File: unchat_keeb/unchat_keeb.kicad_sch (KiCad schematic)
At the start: 11 parts, among them U1 74HC365, U2 74HC365, U3 74HC365, U4 74HC365, U5 74HC365, U6 74HC365, U99 Raspberry_Pi_Pico

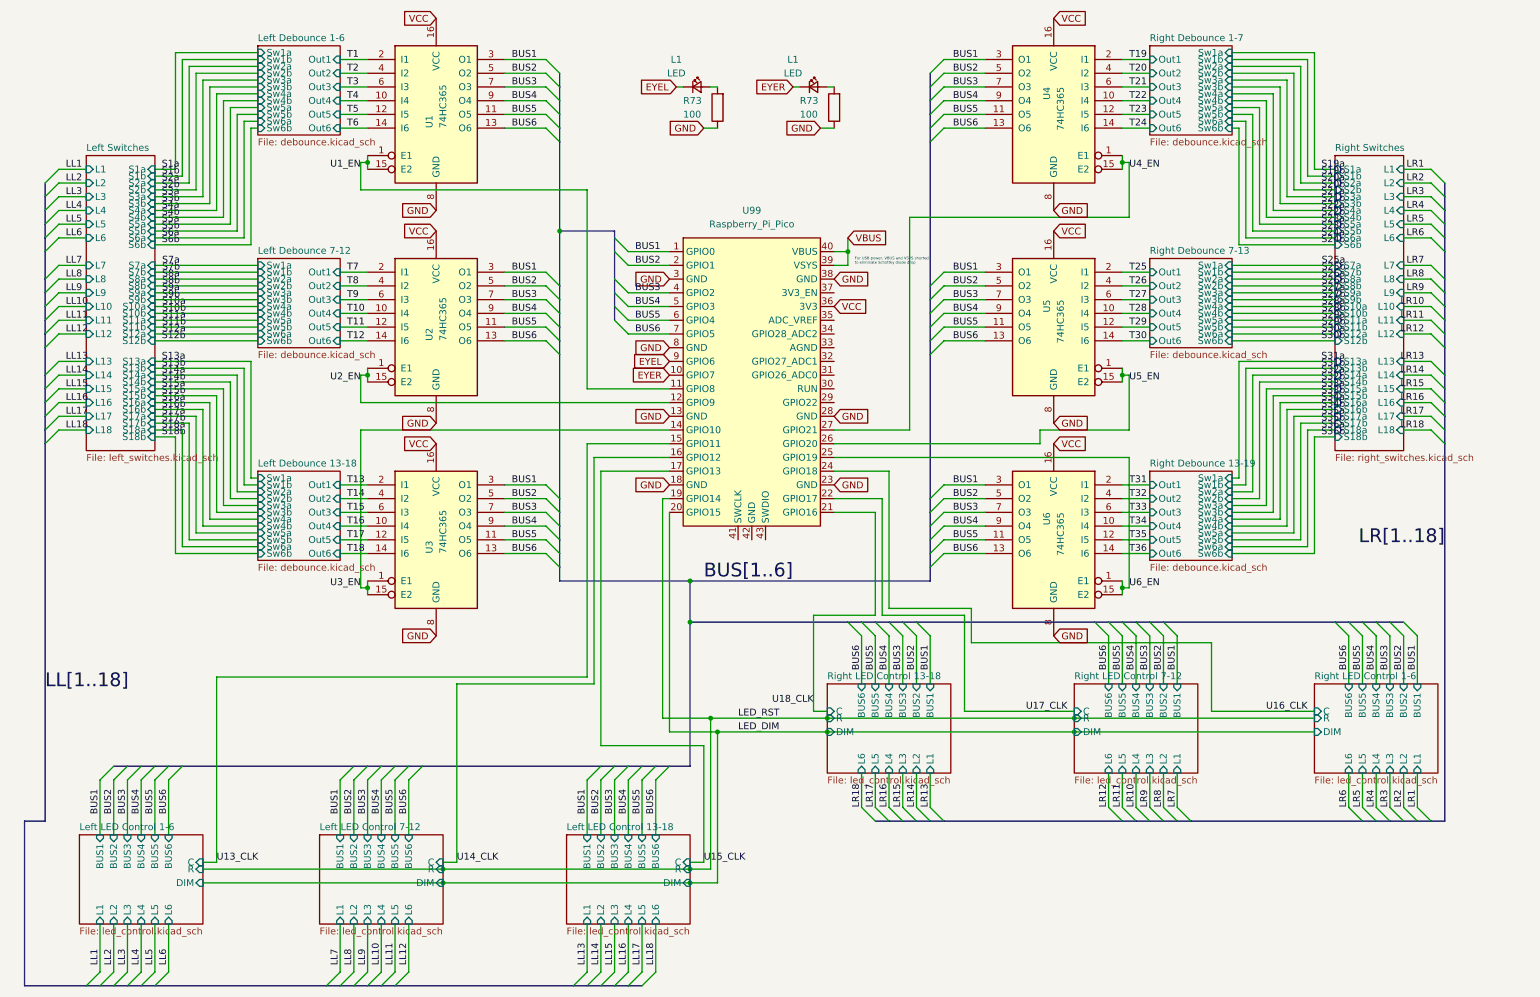
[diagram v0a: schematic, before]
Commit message: Add extra columns, updating to 42-key design
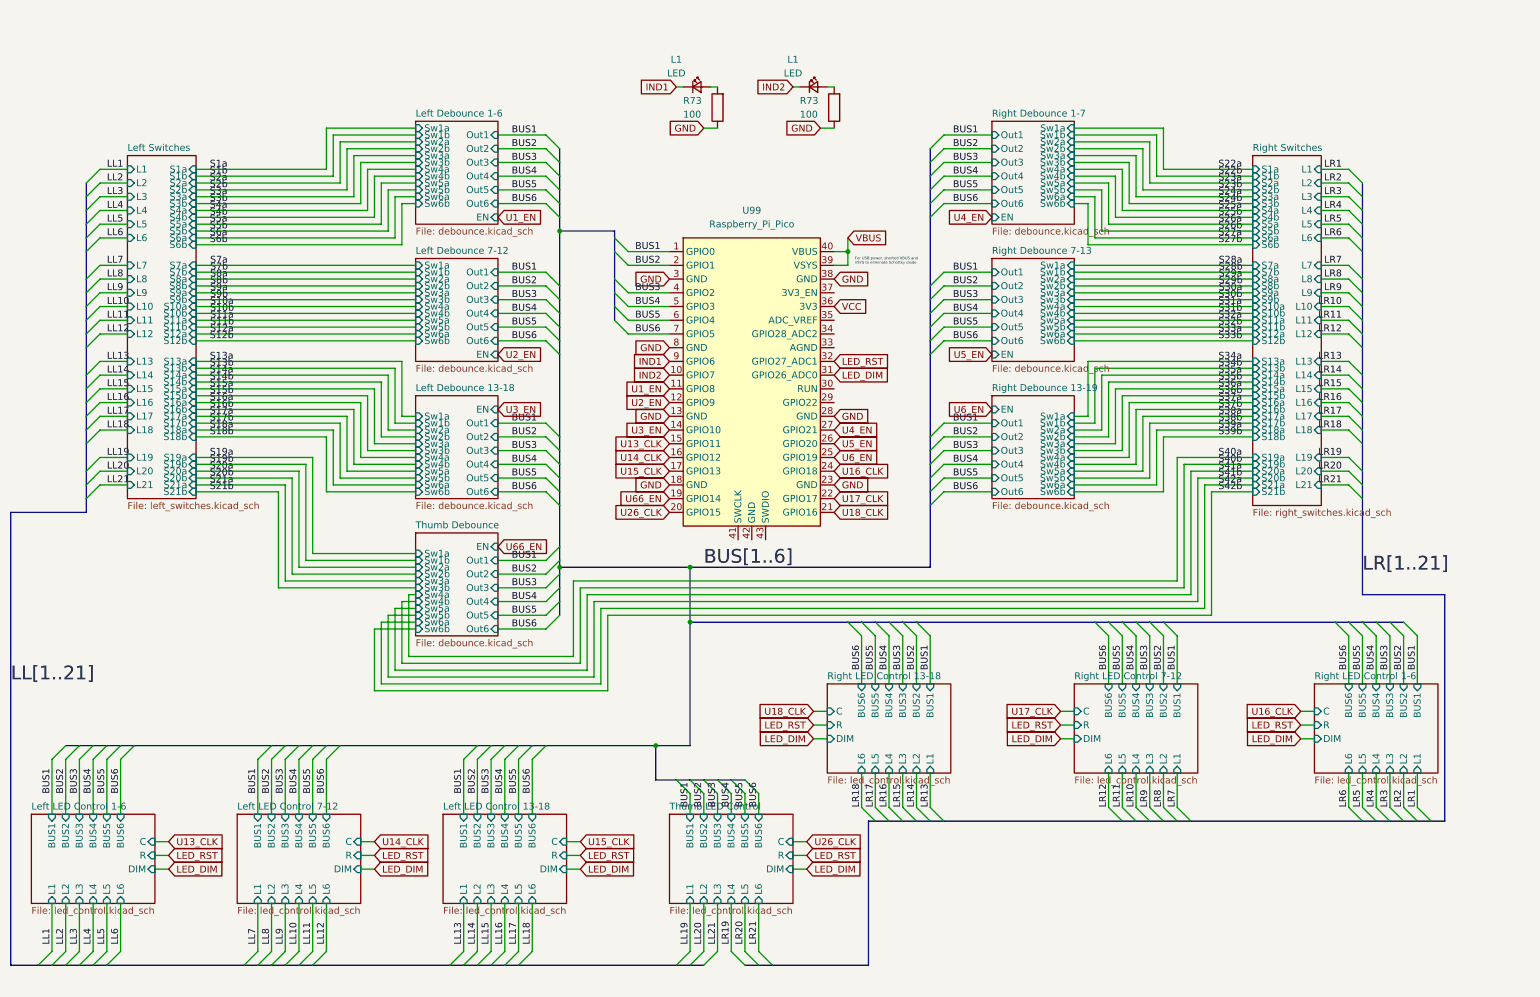
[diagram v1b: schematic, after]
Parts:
- removed U1, U2, U3, U4, U5, U6: 74HC365, Package_SO:TSSOP-16_4.4x5mm_P0.65mm, symbol 74xx:74LS365
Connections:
- net LED_DIM: now also U99.31 (GPIO26_ADC0); no longer U99.20 (GPIO15)
- net LED_RST: now also U99.32 (GPIO27_ADC1); no longer U99.19 (GPIO14)
- net EYEL renamed IND1
- net EYER renamed IND2
- net T31 renamed U6_EN
- new net U26_CLK: U99.20 (GPIO15)
- new net U66_EN: U99.19 (GPIO14)
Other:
- added sheet Thumb Debounce (debounce.kicad_sch)
- added sheet Thumb LED Control (led_control.kicad_sch)
- sheet Left Debounce 1-6 ports: added EN; removed none
- sheet Left Debounce 13-18 ports: added EN; removed none
- sheet Left Debounce 7-12 ports: added EN; removed none
- sheet Left Switches ports: added L19, L20, L21, S19a, S19b, S20a, S20b, S21a, S21b; removed none
- sheet Right Debounce 1-7 ports: added EN; removed none
- sheet Right Debounce 13-19 ports: added EN; removed none
- sheet Right Debounce 7-13 ports: added EN; removed none
- sheet Right Switches ports: added L19, L20, L21, S19a, S19b, S20a, S20b, S21a, S21b; removed none
- note added: "For USB power, shorted VBUS and VSYS to eliminate Schottky diode"
- note removed: "For USB power, VBUS and VSYS shorted to eliminate Schottky diode drop"
- title: UnChat 36-key Fixed Board -> UnChat 42-key Fixed Board

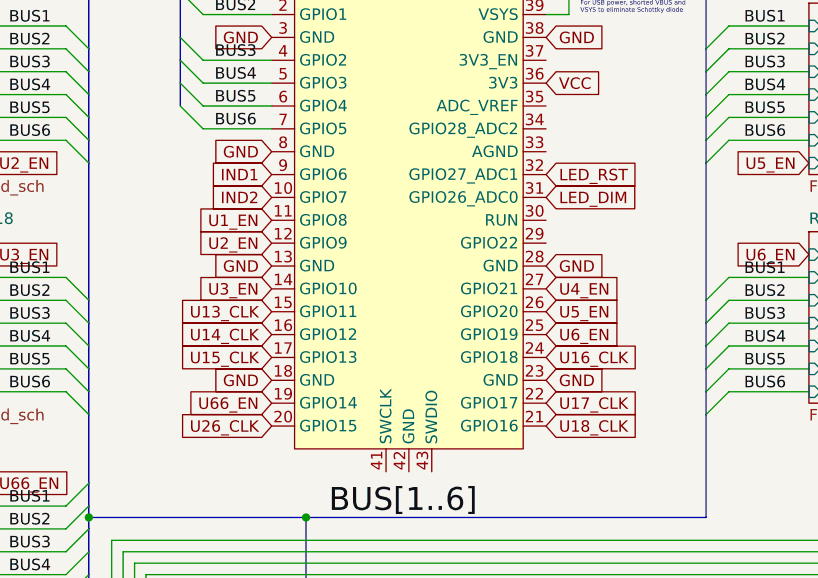
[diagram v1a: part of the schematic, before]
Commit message: Add dxf layout and finish half keyboard pbc layout
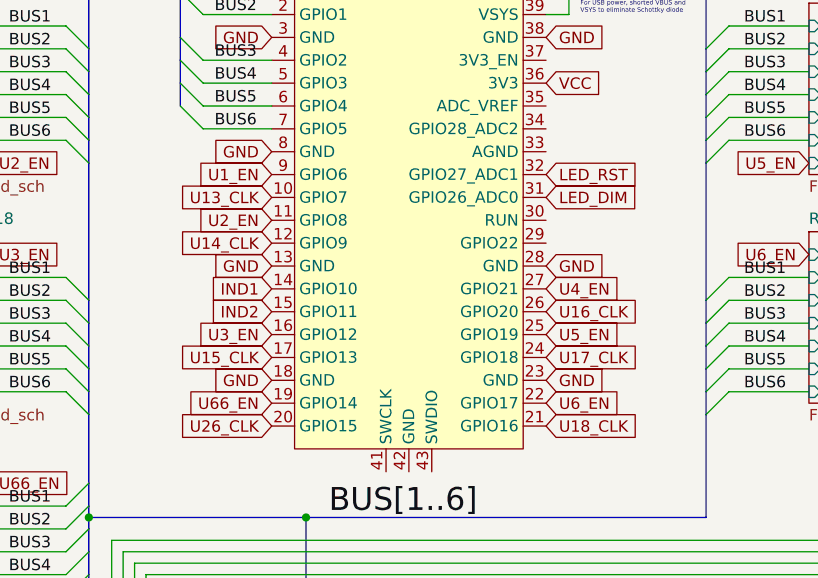
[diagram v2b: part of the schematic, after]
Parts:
- U99: footprint ScottoKeebs_MCU:Raspberry_Pi_Pico -> ScottoKeebs_MCU:Raspberry_Pi_Pico_SMD
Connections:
- net IND1: now also U99.14 (GPIO10); no longer U99.9 (GPIO6)
- net IND2: now also U99.15 (GPIO11); no longer U99.10 (GPIO7)
- net U13_CLK: now also U99.10 (GPIO7); no longer U99.15 (GPIO11)
- net U14_CLK: now also U99.12 (GPIO9); no longer U99.16 (GPIO12)
- net U16_CLK: now also U99.26 (GPIO20); no longer U99.24 (GPIO18)
- net U17_CLK: now also U99.24 (GPIO18); no longer U99.22 (GPIO17)
- net U1_EN: now also U99.9 (GPIO6); no longer U99.11 (GPIO8)
- net U2_EN: now also U99.11 (GPIO8); no longer U99.12 (GPIO9)
- net U3_EN: now also U99.16 (GPIO12); no longer U99.14 (GPIO10)
- net U5_EN: now also U99.25 (GPIO19); no longer U99.26 (GPIO20)
- net U6_EN: now also U99.22 (GPIO17); no longer U99.25 (GPIO19)

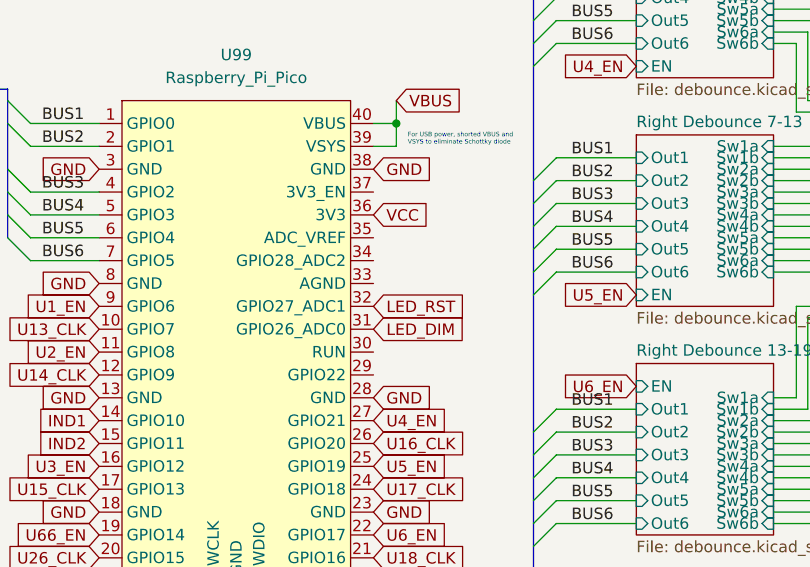
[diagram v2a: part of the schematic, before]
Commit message: Route remaining components, except VCC and GND
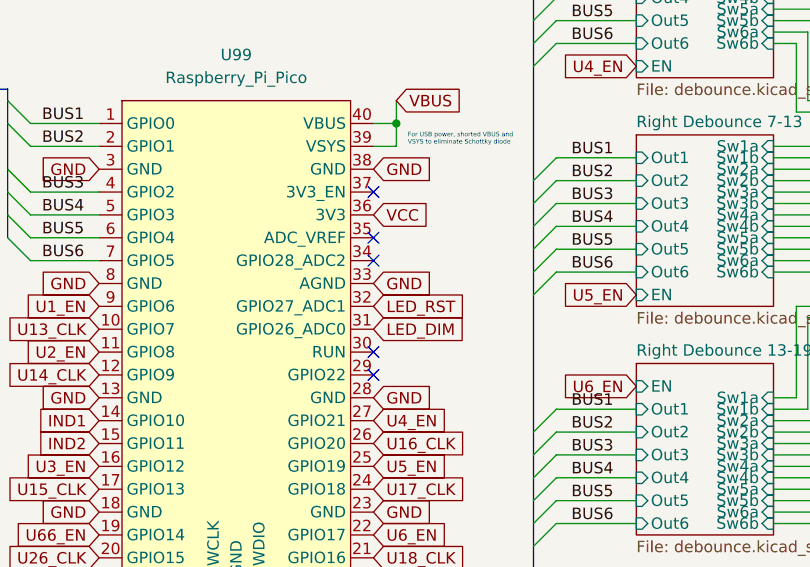
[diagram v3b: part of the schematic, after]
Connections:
- net GND: now also U99.33 (AGND)
- no-connect marks 0 -> 5
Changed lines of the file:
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@@
   (junction (at 133.35 152.4) (diameter 0) (color 0 0 0 0)
   )
+  (no_connect (at 166.37 86.36))
+  (no_connect (at 166.37 88.9))
+  (no_connect (at 166.37 76.2))
+  (no_connect (at 166.37 73.66))
+  (no_connect (at 166.37 68.58))
   (bus_entry (at 264.16 86.36) (size -2.54 -2.54)
     (stroke (width 0) (type default))
@@
     )
   )
+  (global_label "GND" (shape input) (at 166.37 78.74 0) (fields_autoplaced)
+    (effects (font (size 1.27 1.27)) (justify left))
+    (property "Intersheetrefs" "${INTERSHEET_REFS}" (at 173.2257 78.74 0)
+      (effects (font (size 1.27 1.27)) (justify left) hide)
+    )
+  )

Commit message: Finalize the board
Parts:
- added C3 (x8): 0.1uF, Capacitor_SMD:C_0805_2012Metric, symbol Device:C
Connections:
- net GND: now also U99.42 (GND), C3.2, C3.2, C3.2, C3.2, C3.2, C3.2, C3.2, C3.2
- net VCC: now also C3.1, C3.1, C3.1, C3.1, C3.1, C3.1, C3.1, C3.1
- no-connect marks 5 -> 7

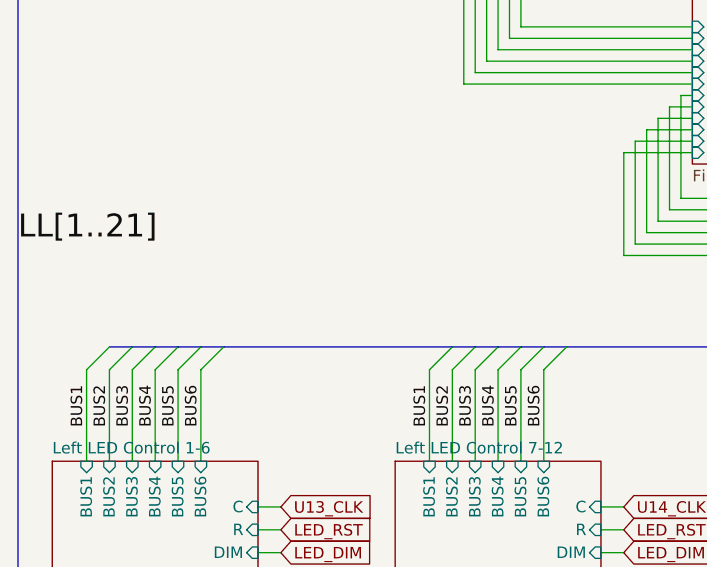
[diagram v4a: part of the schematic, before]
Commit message: Add bus pullups, still need to route 'em
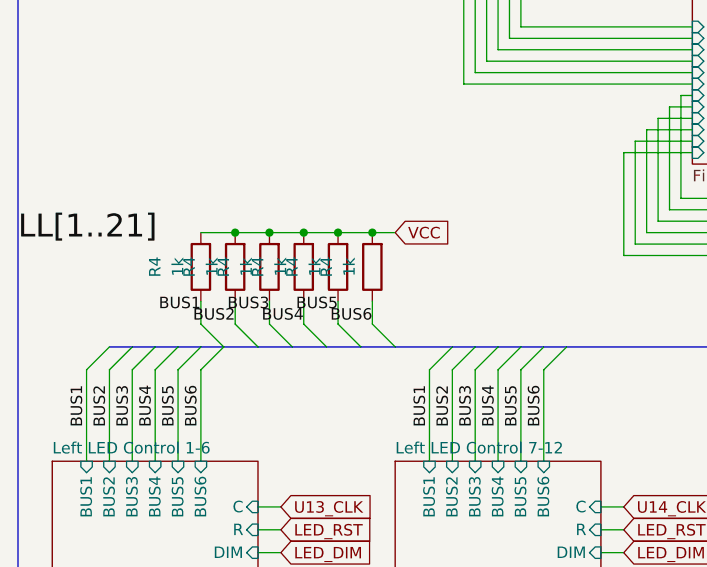
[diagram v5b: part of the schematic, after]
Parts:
- added R4 (x6): 1k, Resistor_SMD:R_0805_2012Metric, symbol ScottoKeebs:Placeholder_Resistor
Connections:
- net BUS1: now also R4.1
- net BUS2: now also R4.1
- net BUS3: now also R4.1
- net BUS4: now also R4.1
- net BUS5: now also R4.1
- net BUS6: now also R4.1
- net VCC: now also R4.2, R4.2, R4.2, R4.2, R4.2, R4.2

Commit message: Remove pullups, as RPi GPIOs are pulled by default
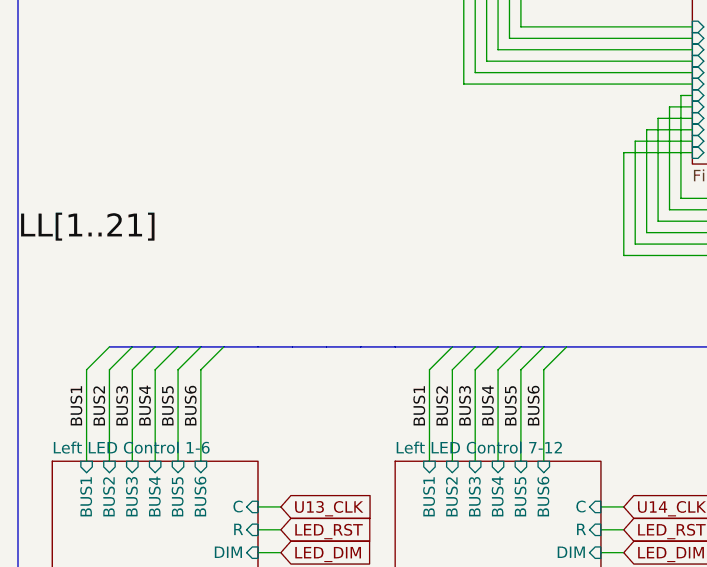
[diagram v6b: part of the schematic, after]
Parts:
- removed R4 (x6): 1k, Resistor_SMD:R_0805_2012Metric, symbol ScottoKeebs:Placeholder_Resistor

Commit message: readme: Added with many images and a snippet of the timelapse
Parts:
- renumbered C3 to C43, C3 to C44, C3 to C45, C3 to C46, C3 to C47, C3 to C48, C3 to C49, C3 to C50, L1 to L37, L1 to L38, R73 to R109, R73 to R110
